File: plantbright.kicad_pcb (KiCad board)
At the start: 2 copper layers, 24 parts, among them J1 POWER OUT, J2 SPEAKER, J4 5V IN, Q1 AO3400A, Q2 AO3400A, Q3 AO3400A, Q4 AO3400A, Q5 AO3400A, SW1 USER 0, SW2 USER 1, U1 XIAO-ESP32-C6, U2 DFPLAYER MINI

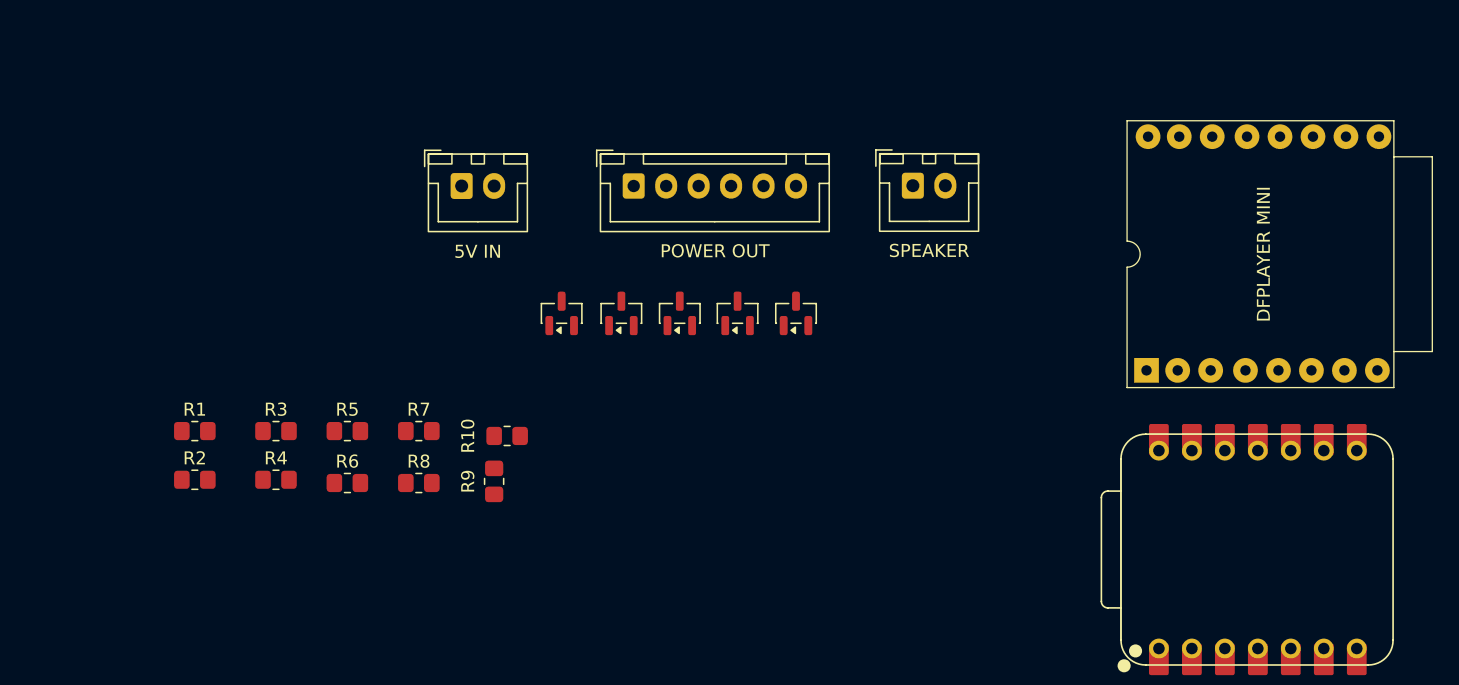
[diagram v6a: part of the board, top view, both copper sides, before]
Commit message: Add C6 text to silkscreen
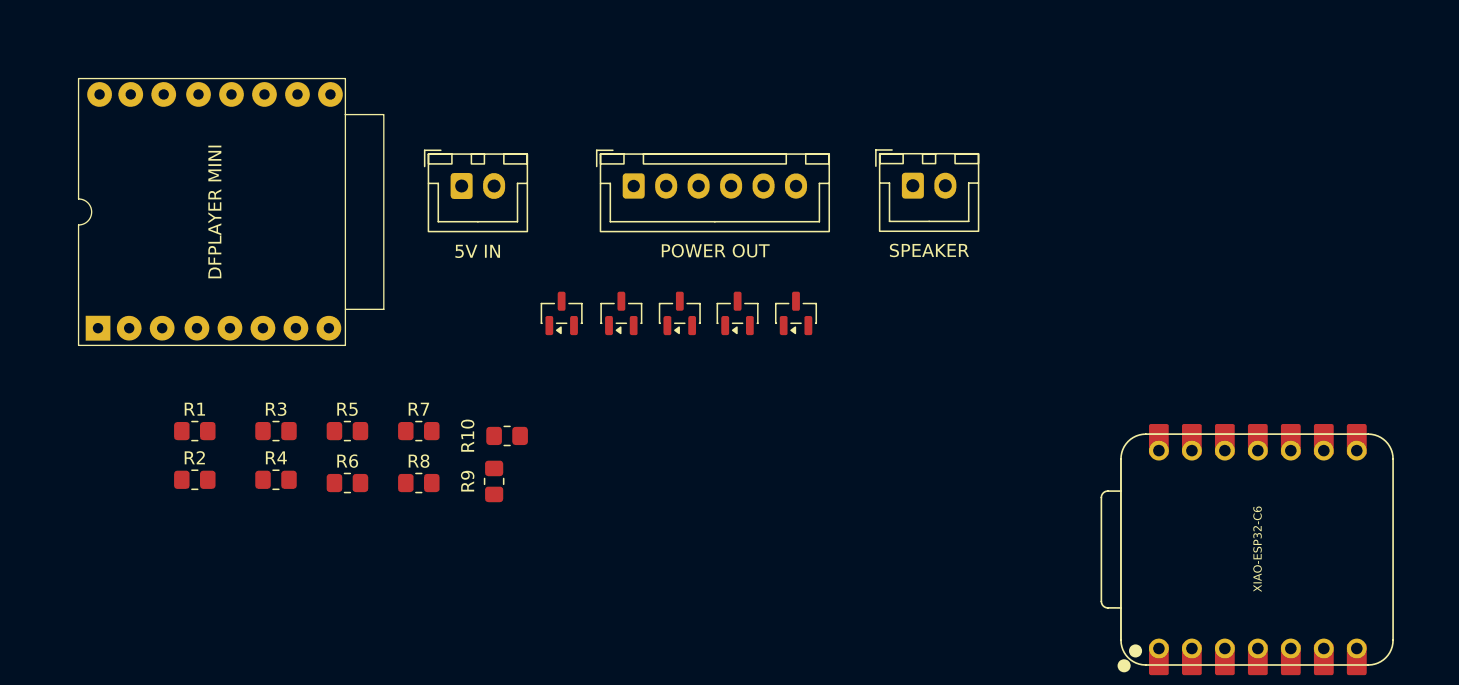
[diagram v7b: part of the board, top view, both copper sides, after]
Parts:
- moved U2 80.8 mm to (113.5, 69.2)
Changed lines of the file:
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@@
 	(footprint "kicad-dfplayermini:dfplayer"
 		(layer "F.Cu")
-		(at 194.28005 72.5 90)
+		(at 113.53005 69.25 90)
 		(property "Reference" "U2"
 			(at 0 2.05 90)
@@
 			(at 0 0 90)
 			(unlocked yes)
-			(layer "F.Fab")
-			(hide yes)
-			(effects
-				(font
+			(layer "F.SilkS")
+			(effects
+				(font

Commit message: Enough for today.
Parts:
- added REF**: MountingHole_3.2mm_M3_DIN965_Pad_TopOnly, MountingHole:MountingHole_3.2mm_M3_DIN965_Pad_TopOnly, F.Cu at (196.0, 51.5)
- added REF**: MountingHole_3.2mm_M3_DIN965_Pad_TopOnly, MountingHole:MountingHole_3.2mm_M3_DIN965_Pad_TopOnly, F.Cu at (189.2, 51.5)
- added REF**: MountingHole_3.2mm_M3_DIN965_Pad_TopOnly, MountingHole:MountingHole_3.2mm_M3_DIN965_Pad_TopOnly, F.Cu at (182.2, 51.2)
- added REF**: MountingHole_3.2mm_M3_DIN965_Pad_TopOnly, MountingHole:MountingHole_3.2mm_M3_DIN965_Pad_TopOnly, F.Cu at (203.0, 51.8)
- moved R11 166.8 mm to (174.9, 38.9)
- moved R12 166.8 mm to (174.9, 41.9)
- moved SW1 166.8 mm to (164.0, 39.5)
- moved SW2 166.8 mm to (164.0, 48.0)
- moved U2 97.1 mm to (207.5, 93.5)
- moved R7 56.7 mm to (185.2, 77.5)
- moved R8 56.7 mm to (185.2, 81.5)
- moved R1 56.7 mm to (168.0, 77.5)
- moved R2 56.7 mm to (168.0, 81.2)
- moved R3 56.7 mm to (174.2, 77.5)
- moved R4 56.7 mm to (174.2, 81.2)
- moved R5 56.7 mm to (179.8, 77.5)
- moved R6 56.7 mm to (179.8, 81.5)
- moved U1 53.0 mm to (140.8, 94.4), turned to -90 degrees
- moved J4 44.9 mm to (136.0, 112.0), turned to 180 degrees
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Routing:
- net Net-(Q5-G): track 0.00 -> 3.79 mm
